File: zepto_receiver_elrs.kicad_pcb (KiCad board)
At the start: 4 copper layers, 9.5 x 7.5 mm, 43 parts, among them J1 u.fl, SW1 SW_Push, U1 STM32WLE5JBI6, U2 NCP160, U3 BGS12PL6E6327XTSA1, U4 0900FM15D0039, U5 ECS-TXO-25CSMV-320-AM-TR

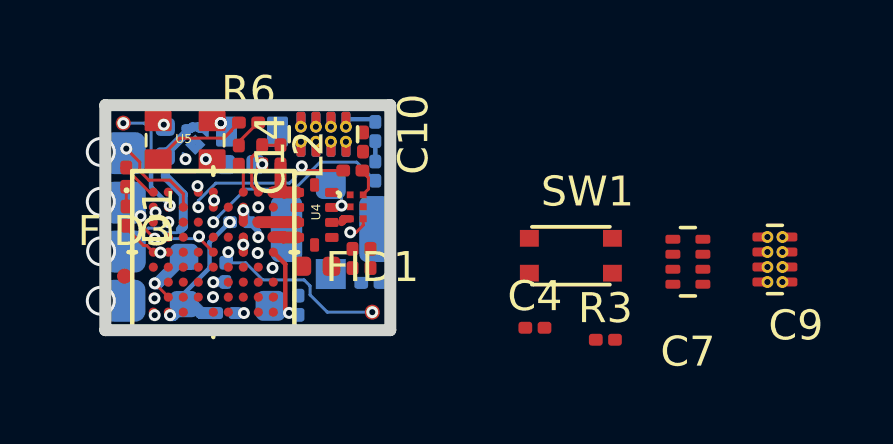
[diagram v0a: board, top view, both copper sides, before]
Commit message: update schematic and layout
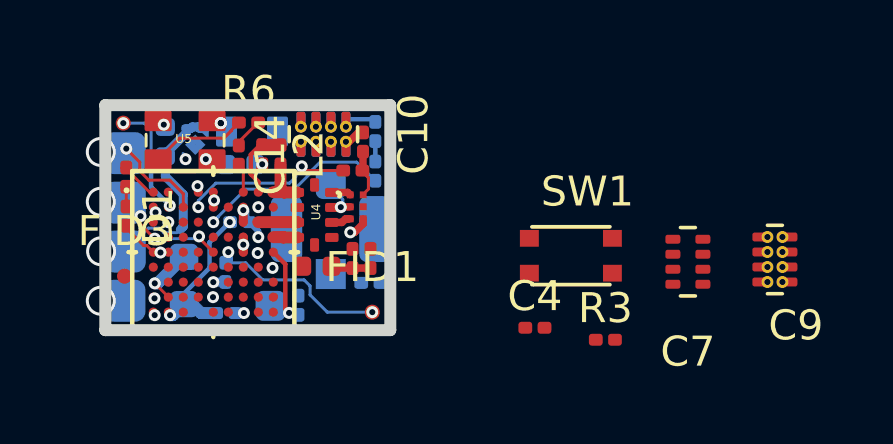
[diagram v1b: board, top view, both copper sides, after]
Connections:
- U1 pad A4: Net-(U1-PadA4) -> SWDCLK
- U1 pad B9: SWDCLK -> Net-(U1-PadB9)
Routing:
- net Net-(C18-Pad2): track 0.00 -> 1.32 mm
- net GND: track 4.50 -> 5.76 mm
- net RFO: track 0.00 -> 0.65 mm
- net Net-(C13-Pad2): track 0.96 -> 1.60 mm

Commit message: moved a few components, checked pinout
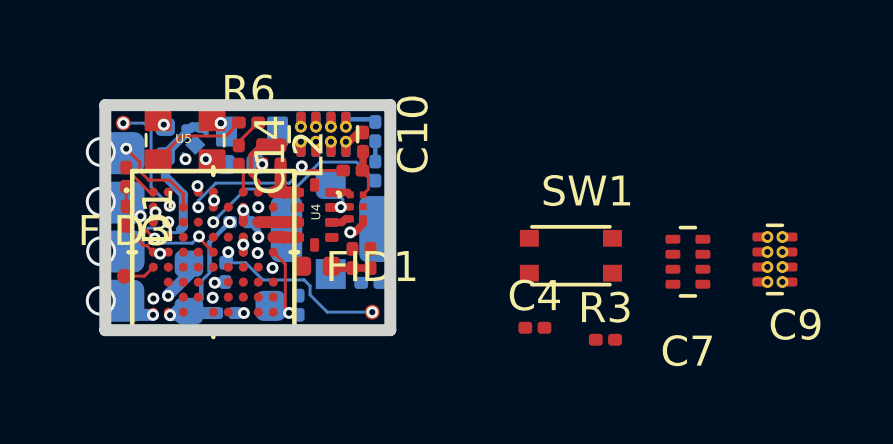
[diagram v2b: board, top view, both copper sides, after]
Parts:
- moved L1 0.28 mm to (123.1, 57.1)
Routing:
- net GND: track 5.76 -> 6.88 mm
- net SWDCLK: track 0.00 -> 1.08 mm
- net Net-(L1-Pad1): track 2.35 -> 1.48 mm

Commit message: update sch, pdf and layout, add 3d views
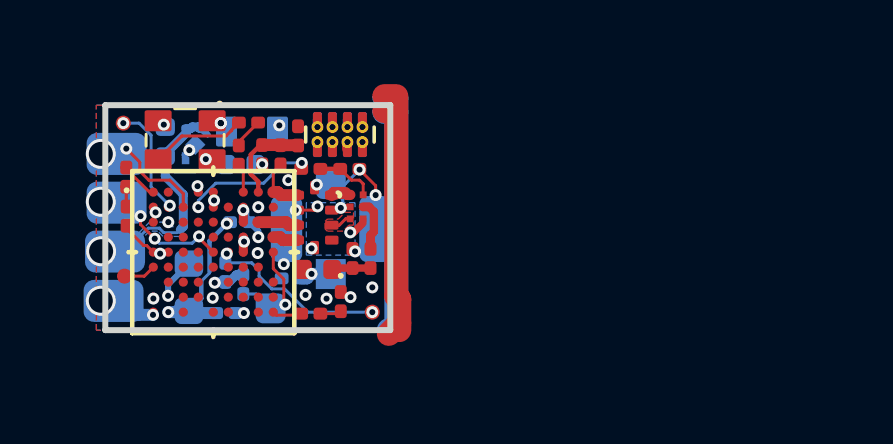
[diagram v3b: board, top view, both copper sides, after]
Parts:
- removed C4: 1µF, ftprnts:C_0201_0603Metric_dense
- removed C7: 2.2uF, ftprnts:0805_low_esl_cap_avx
- removed C9: 2.2uF, ftprnts:0805_low_esl_cap_avx_w_via_dense
- removed R3: 10k, ftprnts:R_0201_0603Metric_dense
- removed SW1: SW_Push, ftprnts:EVPBL9A2B000
- added C15: 68pF, ftprnts:C_0201_0603Metric_dense, F.Cu at (126.7, 52.0)
- C10: moved to B.Cu
- C11, D2, R2: moved to F.Cu
- TP2, TP3, TP4, TP5: footprint TestPoint:TestPoint_Pad_1.5x1.5mm -> ftprnts:TestPoint_Pad_1.5x2mm
- moved D2 5.79 mm to (128.2, 57.5), turned to 270 degrees
- moved R2 5.21 mm to (127.2, 58.0), turned to 180 degrees
- moved C26 2.65 mm to (126.5, 56.8), turned to 180 degrees
- moved R4 1.97 mm to (124.9, 57.0)
- moved R5 1.40 mm to (127.2, 53.1)
- moved C13 1.00 mm to (128.4, 53.1), turned to 180 degrees
- moved TP2 0.58 mm to (120.3, 57.5)
- moved C10 0.55 mm to (128.1, 52.0), turned to 270 degrees
- moved C11 0.55 mm to (128.1, 52.0), turned to 270 degrees
- moved TP3 0.53 mm to (120.4, 55.9)
- moved TP4 0.49 mm to (120.4, 52.6)
- moved TP5 0.48 mm to (120.4, 54.2)
- moved L6 0.11 mm to (127.4, 56.5)
- moved U4 0.09 mm to (127.3, 54.8)
- moved TP1 0.09 mm to (125.8, 57.8)
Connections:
- D2 pad 1: Net-(D2-Pad1) -> GND
- D2 pad 2: +3V3 -> Net-(D2-Pad2)
- R2 pad 1: LED2 -> Net-(D2-Pad2)
- R2 pad 2: Net-(D2-Pad1) -> LED2
- U1 pad E7: LED2 -> Net-(U1-PadE7)
- U1 pad J1: BIND_BUT -> LED2
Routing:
- net GND: track 6.88 -> 28.4 mm, vias 16 -> 28
- net LED2: track 6.53 -> 0.99 mm, vias 1 -> 0
- net Net-(C18-Pad1): track 0.00 -> 1.71 mm
- net RFSW_CRTL: track 5.67 -> 4.19 mm
- net Net-(C26-Pad1): track 0.00 -> 1.11 mm, vias 0 -> 1
- net Net-(D2-Pad2): track 0.00 -> 0.71 mm
- net Net-(D2-Pad1): track 0.68 -> 0.00 mm
- net VR_PA: track 2.53 -> 3.12 mm
- net +3V3: track 5.57 -> 5.54 mm, vias 9 -> 10
- added copper zone on B.Cu, net 3.3-5V_IN
- added copper zone on B.Cu, net GND
- added copper zone on F.Cu, net GND
- added copper zone on F.Cu, net RFI

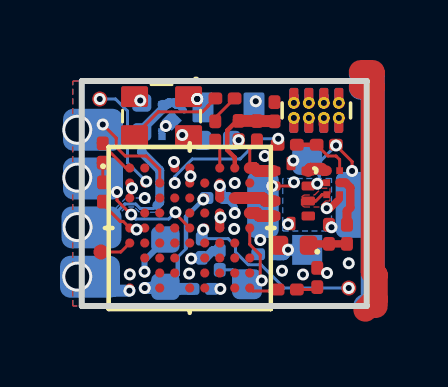
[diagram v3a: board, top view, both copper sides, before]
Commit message: Created panels, changed sideplating, added a few comments
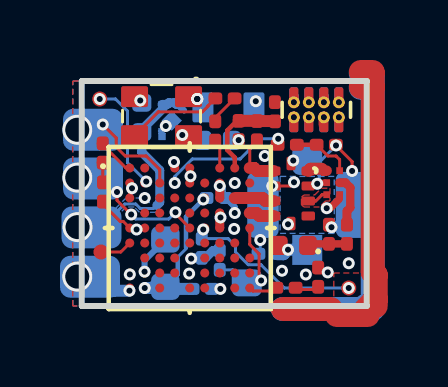
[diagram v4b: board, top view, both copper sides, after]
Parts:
- moved R2 0.07 mm to (127.1, 57.9)
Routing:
- net GND: track 28.4 -> 47.6 mm
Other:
- board text added: "Castellated pads"
- board text added: "Sideplating"
